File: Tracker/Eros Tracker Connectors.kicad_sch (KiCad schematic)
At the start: 1 part, among them P1 USB_C_Plug_USB2.0

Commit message: Midway through board layout
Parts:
- removed P1: USB_C_Plug_USB2.0, symbol Connector:USB_C_Plug_USB2.0
- added J1: 2171790001, 2171790001_MOL, symbol Eros Tracker:2171790001
- added J10, J11, J8, J9: ~, Eros Tracker:10mmDisc, symbol Eros Tracker:Power_Pad
- added J2: S8B-PH-SM4-TB(LF)(SN), Eros Tracker:S8BPHSM4TBLFSN, symbol Eros Tracker:S8B-PH-SM4-TB_LF__SN_
- added J3: S2B-PH-SM4-TB(LF)(SN), Eros Tracker:S2BPHSM4TBLFSN, symbol Eros Tracker:S2B-PH-SM4-TB_LF__SN_
- added J4, J5, J6, J7: 24881, Eros Tracker:2488x-NPTH, symbol Eros Tracker:24881
- added R13 (x2): 5k1, Resistor_SMD:R_0805_2012Metric, symbol Device:R_US
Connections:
- net GND: now also J1.13 (Shield), J1.14 (Shield), J1.15 (Shield), J1.16 (Shield), J1.A1/B12 (GND), J1.B1/A12 (GND), J11.1, J2.6, J2.MP1, J2.MP2, J3.1, J3.MP1, J3.MP2, R13.2, R13.2
- net I2C_SCL: now also J2.5
- net I2C_SDA: now also J2.3
- net INT: now also J2.1
- net USB_D+: now also J1.A6 (DP1), J1.B6 (DP2)
- net USB_D-: now also J1.A7 (DN1), J1.B7 (DN2)
- net VBUS: now also J1.A4/B9 (VBUS), J1.B4/A9 (VBUS)
- net ~{RESET}: now also J2.2
- new net: J1.A5 (CC1), R13.1
- new net: J1.B5 (CC2), R13.1
- new net +3V3: J2.4
- new net +BATT: J3.2
- new net +EXT_MOTOR: J2.7
- new net -EXT_MOTOR: J2.8
- new net POWER_VIN1: J4.1, J5.1
- new net POWER_VIN2: J6.1, J7.1
- new net VBUS_OUT: J8.1
- no-connect marks 0 -> 4

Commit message: Alpha release
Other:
- moved on the sheet: J10, J11, J8, J9
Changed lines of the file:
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@@
   )
   (no_connect (at 52.07 53.34))
-  (no_connect (at 256.54 113.03))
-  (no_connect (at 237.49 121.92))
+  (no_connect (at 240.03 116.84))
+  (no_connect (at 220.98 125.73))
   (no_connect (at 92.71 55.88))
   (wire (pts (xy 83.82 107.95) (xy 83.82 105.41))
@@
   )
   (text_box "Place power pads/strike plates directly concentric with the standoffs on the other side, with J8 and J11 diagonally opposite\n"
-    (at 218.44 133.35 0) (size 50.8 11.43)
+    (at 201.93 137.16 0) (size 50.8 11.43)
     (stroke (width 0) (type default))
     (fill (type none))
@@
     (effects (font (size 1.27 1.27)) (justify right))
   )
-  (hierarchical_label "VBUS_OUT" (shape input) (at 237.49 113.03 180) (fields_autoplaced)
+  (hierarchical_label "VBUS_OUT" (shape input) (at 220.98 116.84 180) (fields_autoplaced)
     (effects (font (size 1.27 1.27)) (justify right))
   )
@@
     )
   )
-  (symbol (lib_id "Eros Tracker:Power_Pad") (at 240.03 113.03 0) (unit 1)
-    (in_bom yes) (on_board yes) (dnp no) (fields_autoplaced)
-    (property "Reference" "J8" (at 242.57 113.665 0)
-      (effects (font (size 1.27 1.27)) (justify left))
-    )
-    (property "Value" "~" (at 240.03 113.03 0)
-      (effects (font (size 1.27 1.27)))
-    )
-    (property "Footprint" "Eros Tracker:10mmDisc" (at 240.03 113.03 0)
-      (effects (font (size 1.27 1.27)) hide)
-    )
-    (property "Datasheet" "https://totalelement.com/collections/steel-discs/products/3-8-inch-steel-disc-blank-metal-strike-plates-250-pack" (at 240.03 113.03 0)
+  (symbol (lib_id "Eros Tracker:Power_Pad") (at 223.52 116.84 0) (unit 1)
+    (in_bom yes) (on_board yes) (dnp no) (fields_autoplaced)
+    (property "Reference" "J8" (at 226.06 117.475 0)
+      (effects (font (size 1.27 1.27)) (justify left))
+    )
+    (property "Value" "~" (at 223.52 116.84 0)
+      (effects (font (size 1.27 1.27)))
+    )
+    (property "Footprint" "Eros Tracker:10mmDisc" (at 223.52 116.84 0)
+      (effects (font (size 1.27 1.27)) hide)
+    )
+    (property "Datasheet" "https://totalelement.com/collections/steel-discs/products/3-8-inch-steel-disc-blank-metal-strike-plates-250-pack" (at 223.52 116.84 0)
       (effects (font (size 1.27 1.27)) hide)
     )
@@
     )
   )
-  (symbol (lib_id "Eros Tracker:Power_Pad") (at 240.03 121.92 0) (unit 1)
-    (in_bom yes) (on_board yes) (dnp no) (fields_autoplaced)
-    (property "Reference" "J9" (at 242.57 122.555 0)
-      (effects (font (size 1.27 1.27)) (justify left))
-    )
-    (property "Value" "~" (at 240.03 121.92 0)
-      (effects (font (size 1.27 1.27)))
-    )
-    (property "Footprint" "Eros Tracker:10mmDisc" (at 240.03 121.92 0)
-      (effects (font (size 1.27 1.27)) hide)
-    )
-    (property "Datasheet" "https://totalelement.com/collections/steel-discs/products/3-8-inch-steel-disc-blank-metal-strike-plates-250-pack" (at 240.03 121.92 0)
+  (symbol (lib_id "Eros Tracker:Power_Pad") (at 223.52 125.73 0) (unit 1)
+    (in_bom yes) (on_board yes) (dnp no) (fields_autoplaced)
+    (property "Reference" "J9" (at 226.06 126.365 0)
+      (effects (font (size 1.27 1.27)) (justify left))
+    )
+    (property "Value" "~" (at 223.52 125.73 0)
+      (effects (font (size 1.27 1.27)))
+    )
+    (property "Footprint" "Eros Tracker:10mmDisc" (at 223.52 125.73 0)
+      (effects (font (size 1.27 1.27)) hide)
+    )
+    (property "Datasheet" "https://totalelement.com/collections/steel-discs/products/3-8-inch-steel-disc-blank-metal-strike-plates-250-pack" (at 223.52 125.73 0)
       (effects (font (size 1.27 1.27)) hide)
     )
@@
     )
   )
-  (symbol (lib_id "Eros Tracker:Power_Pad") (at 259.08 113.03 0) (unit 1)
-    (in_bom yes) (on_board yes) (dnp no) (fields_autoplaced)
-    (property "Reference" "J10" (at 261.62 113.665 0)
-      (effects (font (size 1.27 1.27)) (justify left))
-    )
-    (property "Value" "~" (at 259.08 113.03 0)
-      (effects (font (size 1.27 1.27)))
-    )
-    (property "Footprint" "Eros Tracker:10mmDisc" (at 259.08 113.03 0)
-      (effects (font (size 1.27 1.27)) hide)
-    )
-    (property "Datasheet" "https://totalelement.com/collections/steel-discs/products/3-8-inch-steel-disc-blank-metal-strike-plates-250-pack" (at 259.08 113.03 0)
+  (symbol (lib_id "Eros Tracker:Power_Pad") (at 242.57 116.84 0) (unit 1)
+    (in_bom yes) (on_board yes) (dnp no) (fields_autoplaced)
+    (property "Reference" "J10" (at 245.11 117.475 0)
+      (effects (font (size 1.27 1.27)) (justify left))
+    )
+    (property "Value" "~" (at 242.57 116.84 0)
+      (effects (font (size 1.27 1.27)))
+    )
+    (property "Footprint" "Eros Tracker:10mmDisc" (at 242.57 116.84 0)
+      (effects (font (size 1.27 1.27)) hide)
+    )
+    (property "Datasheet" "https://totalelement.com/collections/steel-discs/products/3-8-inch-steel-disc-blank-metal-strike-plates-250-pack" (at 242.57 116.84 0)
       (effects (font (size 1.27 1.27)) hide)
     )
@@
     )
   )
-  (symbol (lib_id "power:GND") (at 256.54 121.92 0) (unit 1)
-    (in_bom yes) (on_board yes) (dnp no) (fields_autoplaced)
-    (property "Reference" "#PWR049" (at 256.54 128.27 0)
-      (effects (font (size 1.27 1.27)) hide)
-    )
-    (property "Value" "GND" (at 256.54 127 0)
-      (effects (font (size 1.27 1.27)))
-    )
-    (property "Footprint" "" (at 256.54 121.92 0)
-      (effects (font (size 1.27 1.27)) hide)
-    )
-    (property "Datasheet" "" (at 256.54 121.92 0)
+  (symbol (lib_id "power:GND") (at 240.03 125.73 0) (unit 1)
+    (in_bom yes) (on_board yes) (dnp no) (fields_autoplaced)
+    (property "Reference" "#PWR049" (at 240.03 132.08 0)
+      (effects (font (size 1.27 1.27)) hide)
+    )
+    (property "Value" "GND" (at 240.03 130.81 0)
+      (effects (font (size 1.27 1.27)))
+    )
+    (property "Footprint" "" (at 240.03 125.73 0)
+      (effects (font (size 1.27 1.27)) hide)
+    )
+    (property "Datasheet" "" (at 240.03 125.73 0)
       (effects (font (size 1.27 1.27)) hide)
     )
@@
     )
   )
-  (symbol (lib_id "Eros Tracker:Power_Pad") (at 259.08 121.92 0) (unit 1)
-    (in_bom yes) (on_board yes) (dnp no) (fields_autoplaced)
-    (property "Reference" "J11" (at 261.62 122.555 0)
-      (effects (font (size 1.27 1.27)) (justify left))
-    )
-    (property "Value" "~" (at 259.08 121.92 0)
-      (effects (font (size 1.27 1.27)))
-    )
-    (property "Footprint" "Eros Tracker:10mmDisc" (at 259.08 121.92 0)
-      (effects (font (size 1.27 1.27)) hide)
-    )
-    (property "Datasheet" "https://totalelement.com/collections/steel-discs/products/3-8-inch-steel-disc-blank-metal-strike-plates-250-pack" (at 259.08 121.92 0)
-      (effects (font (size 1.27 1.27)) hide)
-    )
+  (symbol (lib_id "Eros Tracker:Power_Pad") (at 242.57 125.73 0) (unit 1)
+    (in_bom yes) (on_board yes) (dnp no) (fields_autoplaced)
+    (property "Reference" "J11" (at 245.11 126.365 0)
+      (effects (font (size 1.27 1.27)) (justify left))
+    )
+    (property "Value" "~" (at 242.57 125.73 0)
+      (effects (font (size 1.27 1.27)))
+    )
+    (property "Footprint" "Eros Tracker:10mmDisc" (at 242.57 125.73 0)
+      (effects (font (size 1.27 1.27)) hide)
+    )
+    (property "Datasheet" "https://totalelement.com/collections/steel-discs/products/3-8-inch-steel-disc-blank-metal-strike-plates-250-pack" (at 242.57 125.73 0)
+      (effects (font (size 1.27 1.27)) hide)
+    )

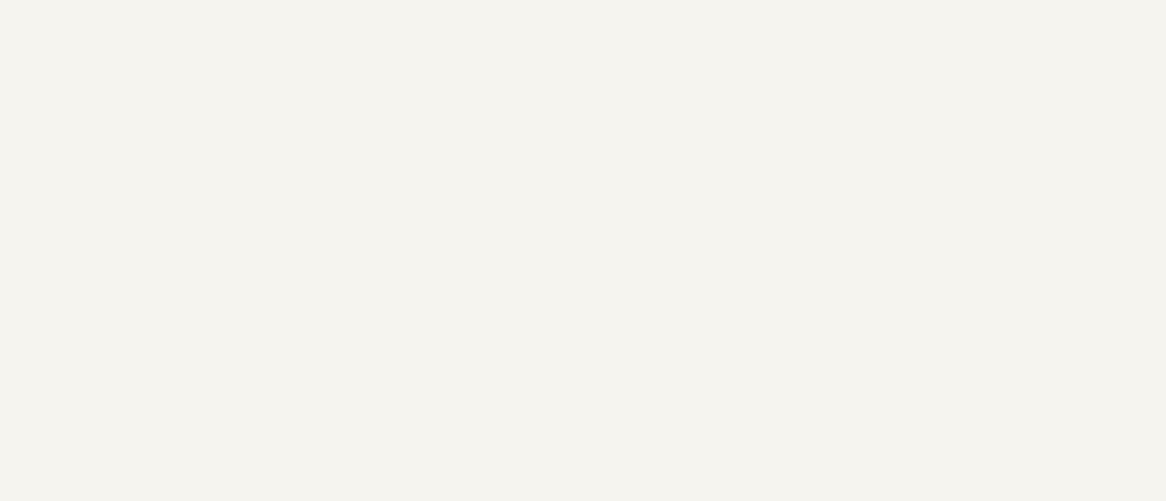
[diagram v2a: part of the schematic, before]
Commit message: Added cuts and jumps for Rev A
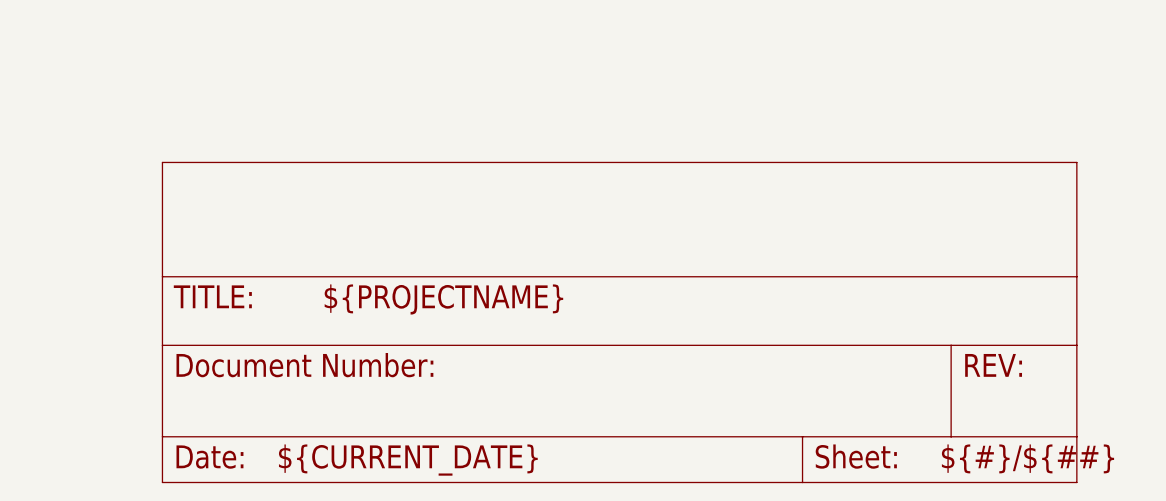
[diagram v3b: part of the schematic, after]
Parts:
- J4, J5, J6, J7: Mouser Price/Stock https://www.mouser.co.uk/ProductDetail/Keystone-Electronics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 -> https://www.mouser.com/ProductDetail/Keystone-Electronics/2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
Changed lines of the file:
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@@
       (effects (font (size 1.27 1.27)) hide)
     )
-    (property "Datasheet" "https://www.mouser.com/datasheet/2/447/PYu_RT_1_to_0_01_RoHS_L_12-3003070.pdf" (at 35.56 45.72 0)
+    (property "Datasheet" "~" (at 35.56 45.72 0)
       (effects (font (size 1.27 1.27)) hide)
     )
@@
         (path "/e762b1f0-85b9-427f-b9a8-4b9d5ef7d00a/d48b8e2f-8217-4d86-802f-6eb46ffa5237"
           (reference "R22") (unit 1)
+        )
+      )
+    )
+  )
+  (symbol (lib_id "Eros Tracker-eagle-import:FRAME_A_L") (at 194.31 209.55 0) (unit 2)
+    (in_bom yes) (on_board yes) (dnp no)
+    (property "Reference" "#FRAME1" (at 194.31 209.55 0)
+      (effects (font (size 1.27 1.27)) hide)
+    )
+    (property "Value" "FRAME_A_L" (at 194.31 209.55 0)
+      (effects (font (size 1.27 1.27)) hide)
+    )
+    (property "Footprint" "" (at 194.31 209.55 0)
+      (effects (font (size 1.27 1.27)) hide)
+    )
+    (property "Datasheet" "" (at 194.31 209.55 0)
+      (effects (font (size 1.27 1.27)) hide)
+    )
+    (instances
+      (project "Eros Tracker"
+        (path "/e762b1f0-85b9-427f-b9a8-4b9d5ef7d00a/9c812c5a-2871-41e5-a7a0-ff8823ff9651"
+          (reference "#FRAME1") (unit 2)
+        )
+        (path "/e762b1f0-85b9-427f-b9a8-4b9d5ef7d00a/d48b8e2f-8217-4d86-802f-6eb46ffa5237"
+          (reference "#FRAME4") (unit 2)
         )
       )
@@
       (effects (font (size 1.27 1.27)) (justify left top) hide)
     )
-    (property "Datasheet" "https://www.keyelco.com/product-pdf.cfm?p=14492" (at 214.63 233.02 0)
+    (property "Datasheet" "https://www.mouser.com/datasheet/2/215/24881-2953526.pdf" (at 214.63 233.02 0)
       (effects (font (size 1.27 1.27)) (justify left top) hide)
     )
@@
       (effects (font (size 1.27 1.27)) (justify left top) hide)
     )
-    (property "Mouser Price/Stock" "https://www.mouser.co.uk/ProductDetail/Keystone-Electronics/24885?qs=u16ybLDytRauJq9rQZt4xg%3D%3D" (at 214.63 633.02 0)
+    (property "Mouser Price/Stock" "https://www.mouser.com/ProductDetail/Keystone-Electronics/24881?qs=u16ybLDytRZRpz%252BqY%2FJM%2FA%3D%3D" (at 214.63 633.02 0)
       (effects (font (size 1.27 1.27)) (justify left top) hide)
     )
@@
       (effects (font (size 1.27 1.27)) (justify left top) hide)
     )
-    (property "Datasheet" "https://www.keyelco.com/product-pdf.cfm?p=14492" (at 214.63 258.42 0)
+    (property "Datasheet" "https://www.mouser.com/datasheet/2/215/24881-2953526.pdf" (at 214.63 258.42 0)
       (effects (font (size 1.27 1.27)) (justify left top) hide)
     )
@@
       (effects (font (size 1.27 1.27)) (justify left top) hide)
     )
-    (property "Mouser Price/Stock" "https://www.mouser.co.uk/ProductDetail/Keystone-Electronics/24885?qs=u16ybLDytRauJq9rQZt4xg%3D%3D" (at 214.63 658.42 0)
+    (property "Mouser Price/Stock" "https://www.mouser.com/ProductDetail/Keystone-Electronics/24881?qs=u16ybLDytRZRpz%252BqY%2FJM%2FA%3D%3D" (at 214.63 658.42 0)
       (effects (font (size 1.27 1.27)) (justify left top) hide)
     )
@@
       (effects (font (size 1.27 1.27)) (justify left top) hide)
     )
-    (property "Datasheet" "https://www.keyelco.com/product-pdf.cfm?p=14492" (at 256.54 258.42 0)
+    (property "Datasheet" "https://www.mouser.com/datasheet/2/215/24881-2953526.pdf" (at 256.54 258.42 0)
       (effects (font (size 1.27 1.27)) (justify left top) hide)
     )
@@
       (effects (font (size 1.27 1.27)) (justify left top) hide)
     )
-    (property "Mouser Price/Stock" "https://www.mouser.co.uk/ProductDetail/Keystone-Electronics/24885?qs=u16ybLDytRauJq9rQZt4xg%3D%3D" (at 256.54 658.42 0)
+    (property "Mouser Price/Stock" "https://www.mouser.com/ProductDetail/Keystone-Electronics/24881?qs=u16ybLDytRZRpz%252BqY%2FJM%2FA%3D%3D" (at 256.54 658.42 0)
       (effects (font (size 1.27 1.27)) (justify left top) hide)
     )
@@
       (effects (font (size 1.27 1.27)) (justify left top) hide)
     )
-    (property "Datasheet" "https://www.keyelco.com/product-pdf.cfm?p=14492" (at 256.54 233.02 0)
+    (property "Datasheet" "https://www.mouser.com/datasheet/2/215/24881-2953526.pdf" (at 256.54 233.02 0)
       (effects (font (size 1.27 1.27)) (justify left top) hide)
     )
@@
       (effects (font (size 1.27 1.27)) (justify left top) hide)
     )
-    (property "Mouser Price/Stock" "https://www.mouser.co.uk/ProductDetail/Keystone-Electronics/24885?qs=u16ybLDytRauJq9rQZt4xg%3D%3D" (at 256.54 633.02 0)
+    (property "Mouser Price/Stock" "https://www.mouser.com/ProductDetail/Keystone-Electronics/24881?qs=u16ybLDytRZRpz%252BqY%2FJM%2FA%3D%3D" (at 256.54 633.02 0)
       (effects (font (size 1.27 1.27)) (justify left top) hide)
     )
@@
       (effects (font (size 1.27 1.27)) hide)
     )
-    (property "Datasheet" "https://www.mouser.com/datasheet/2/447/PYu_RT_1_to_0_01_RoHS_L_12-3003070.pdf" (at 35.56 55.88 0)
-      (effects (font (size 1.27 1.27)) hide)
-    )
+    (property "Datasheet" "~" (at 35.56 55.88 0)
+      (effects (font (size 1.27 1.27)) hide)
+    )
